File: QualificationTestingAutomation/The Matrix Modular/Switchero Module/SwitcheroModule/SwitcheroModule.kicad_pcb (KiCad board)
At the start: 4 copper layers, 87.5 x 78.9 mm, 104 parts, among them IC1 MAX3109ETJ+, J1 Conn_02x32_Counter_Clockwise_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, J2 OBD Connector, J3 OBD Connector, J6 Conn_02x32_Counter_Clockwise_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, Q1 2N7002DW, Q10 2N7002DW, Q2 2N7002DW, Q3 2N7002DW, Q4 2N7002DW, Q5 2N7002DW, Q6 2N7002DW, Q7 2N7002DW, Q8 2N7002DW, Q9 2N7002DW, SW1 SW_DIP_x04, U1 TC2050-JTAG-SchematicAutomati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, U10 TLP3546, U11 TLP3546, U12 CD4070B, U13 MAX324CUA, U14 CD4070B, U15 MAX324CUA, U16 INA181, U17 INA181, U2 AT25SF081-SSHD-X, U3 MSP430G2755IRHA40, U4 SN74HC266DR, U5 SN74LVC08APWR, U6 MAX14752, U7 DG408LE, U8 DS18B20_, U9 DS18B20_

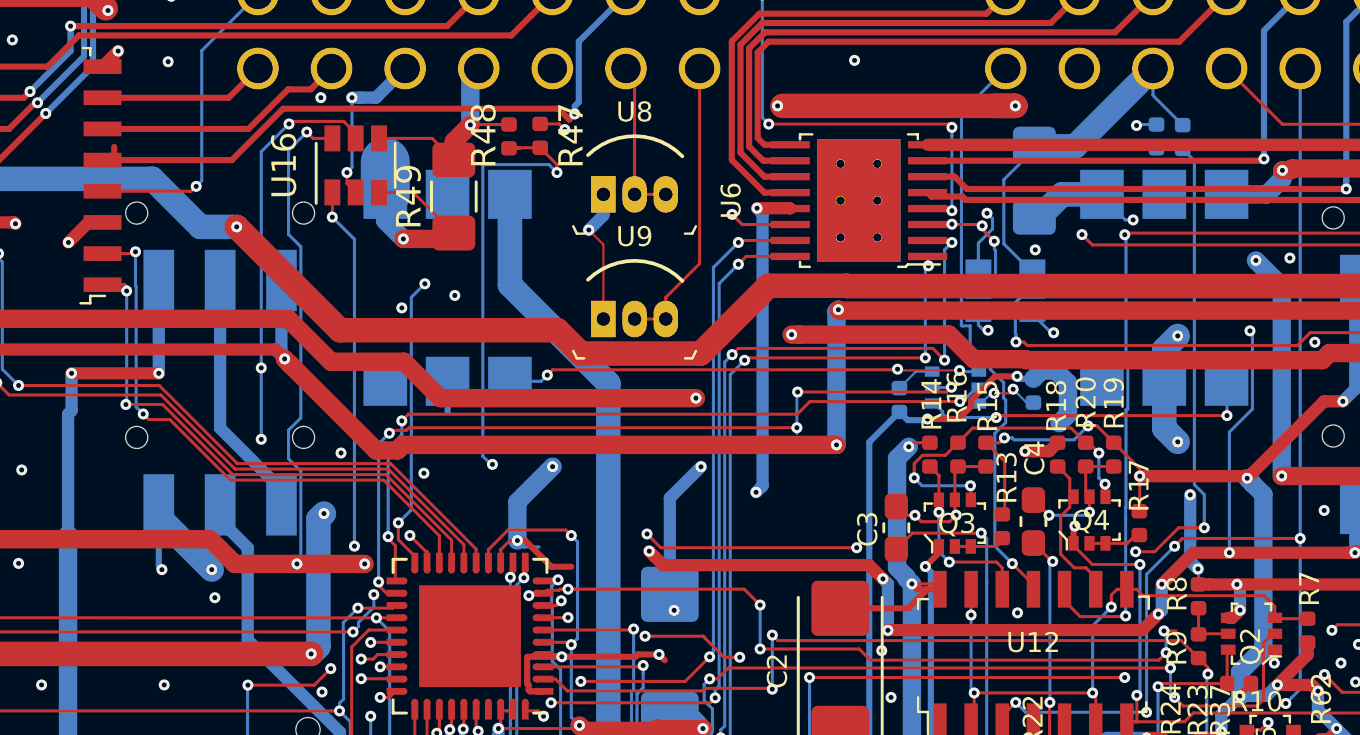
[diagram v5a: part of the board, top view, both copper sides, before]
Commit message: Reefero Module PCB design
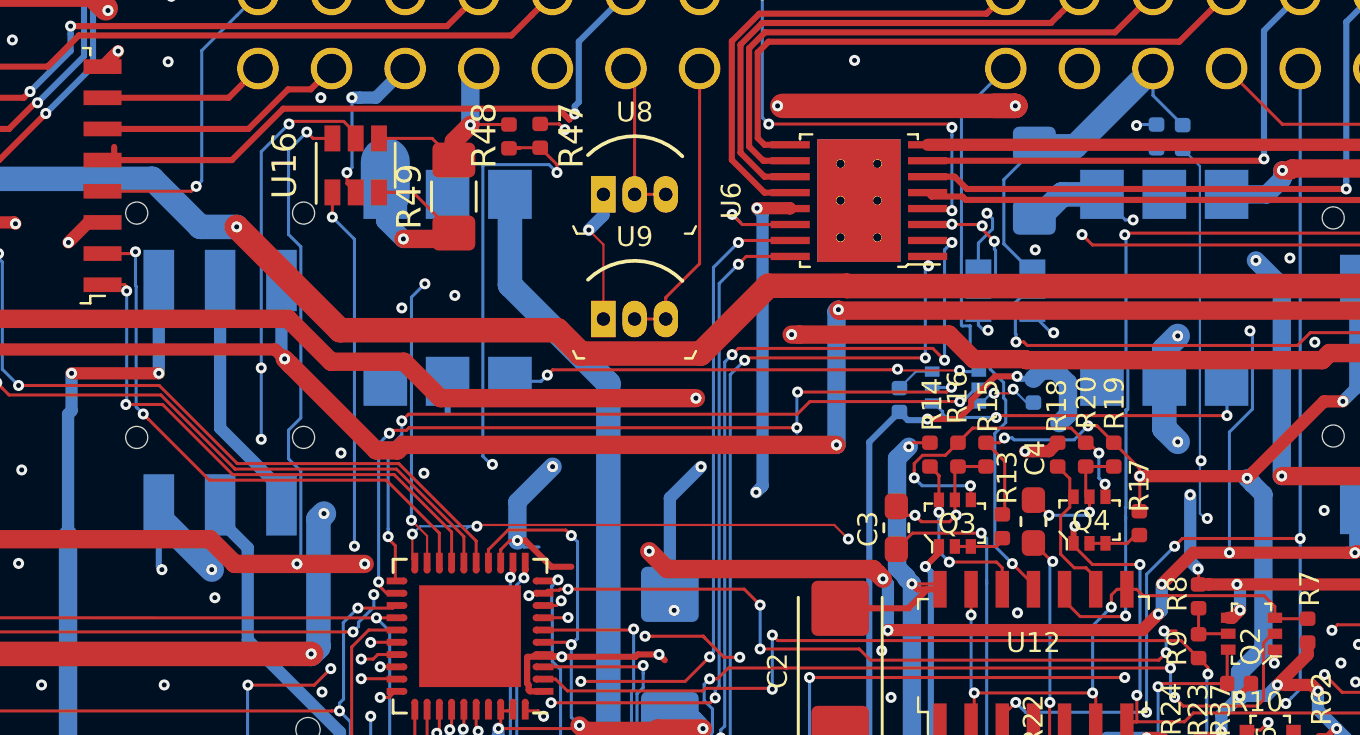
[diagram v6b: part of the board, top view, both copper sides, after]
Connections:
- net /Relays/1_RELH renamed Net-(Q1-Pad1)
- net /Relays/2_RELH renamed Net-(Q1-Pad4)
- net 1_REL renamed MSP_REL_1
- net 2_REL renamed MSP_REL_2
- net A0 renamed VADC_VAA
- net A1 renamed VADC_LO
- net A2 renamed IADC_Vin
- net A5 renamed VADC_Vin
- net MUX1 renamed MSP_MUX1_EN
- net MUX2 renamed MSP_MUX2_EN
- net MUXA renamed MSP_MUXA
- net MUXB renamed MSP_MUXB
- net MUXC renamed MSP_MUXC
- net MUXD renamed MSP_MUXD
- net MUXE renamed MSP_MUXE
- net MUXF renamed MSP_MUXF
- R50 pad 1: A4 -> VADC_Garmin
- R51 pad 1: A4 -> VADC_Garmin
- U17 pad 1: A3 -> IADC_Garmin
- U3 pad 19: A4 -> IADC_Garmin
- U3 pad 20: A3 -> VADC_Garmin
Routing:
- net A4: track 52.3 -> 0.00 mm, vias 5 -> 0
- net VADC_Garmin: track 0.00 -> 51.8 mm, vias 0 -> 5
- net A3: track 36.7 -> 0.00 mm, vias 3 -> 0
- net IADC_Garmin: track 0.00 -> 36.5 mm, vias 0 -> 3
